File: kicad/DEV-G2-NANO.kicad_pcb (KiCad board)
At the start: 6 copper layers, 76.2 x 20.3 mm, 138 parts, among them J1 Lower Bank, J2 Upper Bank, J3 USB C, J4 HIC SWD, J5 RTC Battery, SW1 PTS815, U1 MIMXRT1171DVMAB, U10 TPS62825, U2 MAYA-W166-00B, U3 LSM6DSV, U4 LIS2MDL, U5 RTMC-G2-4IQ48, U6 W25Q64JWUUIQ, U7 MKL26Z128VFM4, U8 LM66200, U9 TPS62086, Y1 8MHz, Y2 16MHz, Y3 24MHz, Y4 32.768kHz

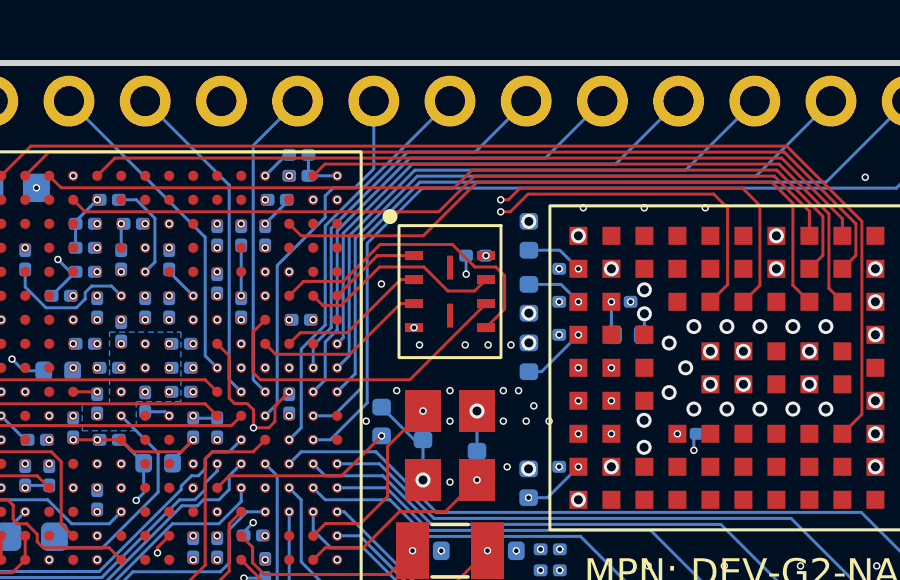
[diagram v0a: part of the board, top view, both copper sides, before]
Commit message: added pull-up resistors to W25Q QSPI line
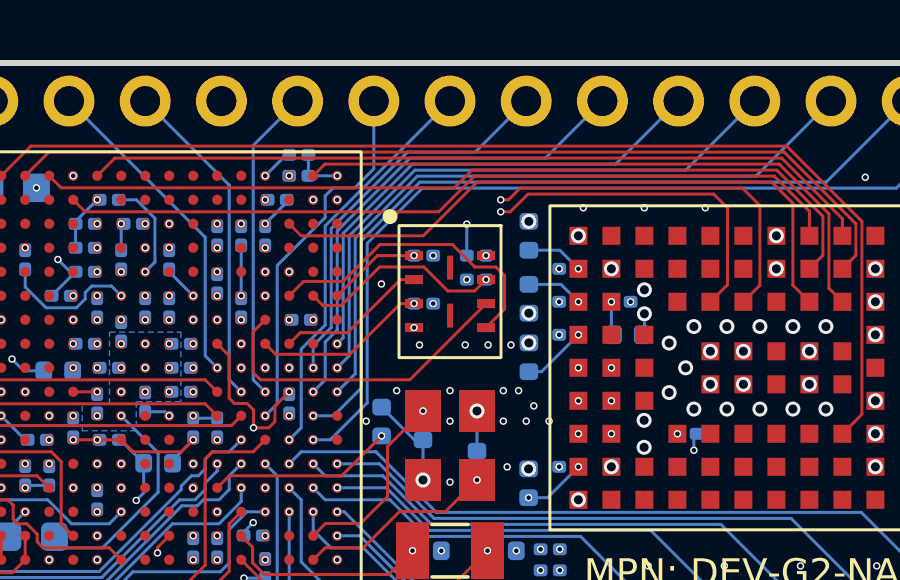
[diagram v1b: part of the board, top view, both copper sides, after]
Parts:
- added R7: 10kΩ, Resistor_SMD:R_0201_0603Metric, B.Cu at (171.1, 87.2)
- added R8: 10kΩ, Resistor_SMD:R_0201_0603Metric, B.Cu at (169.3, 88.0)
- added R9: 10kΩ, Resistor_SMD:R_0201_0603Metric, B.Cu at (169.3, 86.4)
- renumbered R7 to R10, R8 to R11, R9 to R12, R10 to R13, R11 to R14, R12 to R15, R13 to R16, R14 to R17, R15 to R18, R16 to R19, R17 to R20, R18 to R21, R19 to R22, R20 to R23, R21 to R24, R22 to R25, R23 to R26, R24 to R27, R25 to R28, R26 to R29, R27 to R30, R28 to R31, R29 to R32
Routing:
- net +1V8: track 89.2 -> 97.9 mm, vias 26 -> 29
- net Net-(U1B-GPIO_SD_B2_11): vias 0 -> 1
- net Net-(U1B-GPIO_SD_B2_10): vias 0 -> 1
- net Net-(U1B-GPIO_SD_B2_06): vias 0 -> 1

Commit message: cosmetic changes
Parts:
- removed G***: LOGO, LOGO
- added ?: , project_footprints:G2-Nano-Logo, F.Cu at (134.0, 93.6)
- C21, C23, C26: moved to B.Cu
- moved C20 4.35 mm to (141.1, 84.9)
- moved C23 1.71 mm to (136.2, 84.4), turned to 0 degrees
- moved C26 1.69 mm to (136.7, 96.0)
- moved C21 1.67 mm to (139.7, 84.3)
- moved C22 0.73 mm to (140.9, 91.6), turned to 90 degrees
- moved C24 0.16 mm to (132.8, 89.7)
- moved C25 0.16 mm to (132.8, 92.2)
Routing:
- net +3V3: track 13.2 -> 15.5 mm, vias 28 -> 30
- net GND: track 39.2 -> 38.9 mm, vias 215 -> 214
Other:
- board text added: "REV: 1.0"
